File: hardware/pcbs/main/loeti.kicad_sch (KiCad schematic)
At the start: 99 parts, among them J1 REDFIT_SWD_6, J2 DATA, J3 POWER, J4 Conn_01x04_Pin, Q1 Si4162DY, Q2 BC817, Q4 BC817, Q5 BC807, Q6 Si4425FDY, SW1 BOOT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

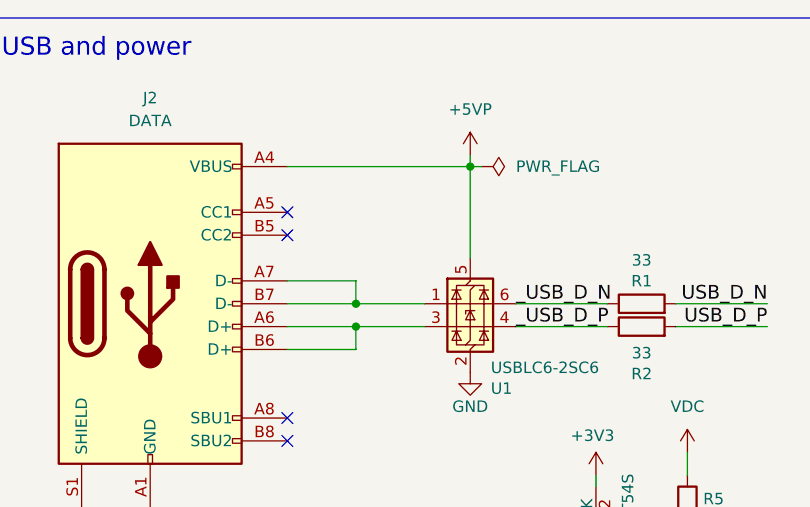
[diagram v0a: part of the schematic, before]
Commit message: fix: v6d hardware, CC resistors on data port
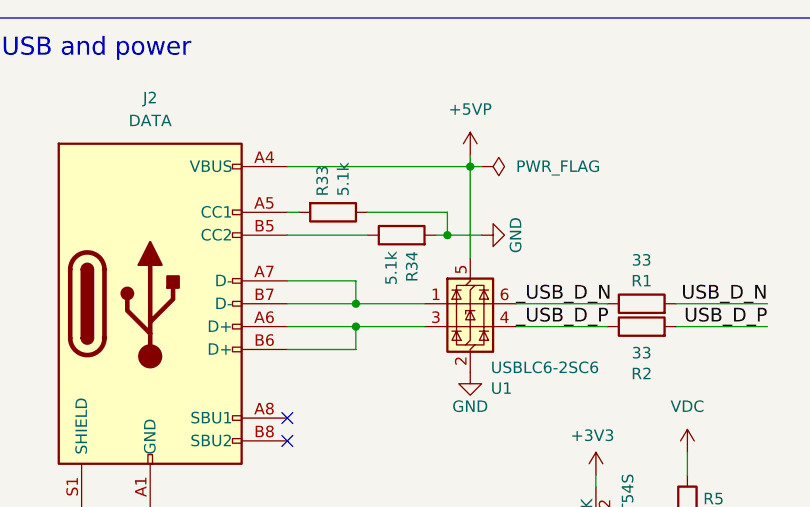
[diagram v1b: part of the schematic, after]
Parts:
- added R33, R34: 5.1k, Resistor_SMD:R_0603_1608Metric, symbol Device:R
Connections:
- net GND: now also R33.1, R34.2
- net at J2.A5 (CC1): now also R33.2
- net at J2.B5 (CC2): now also R34.1
- no-connect marks 22 -> 20

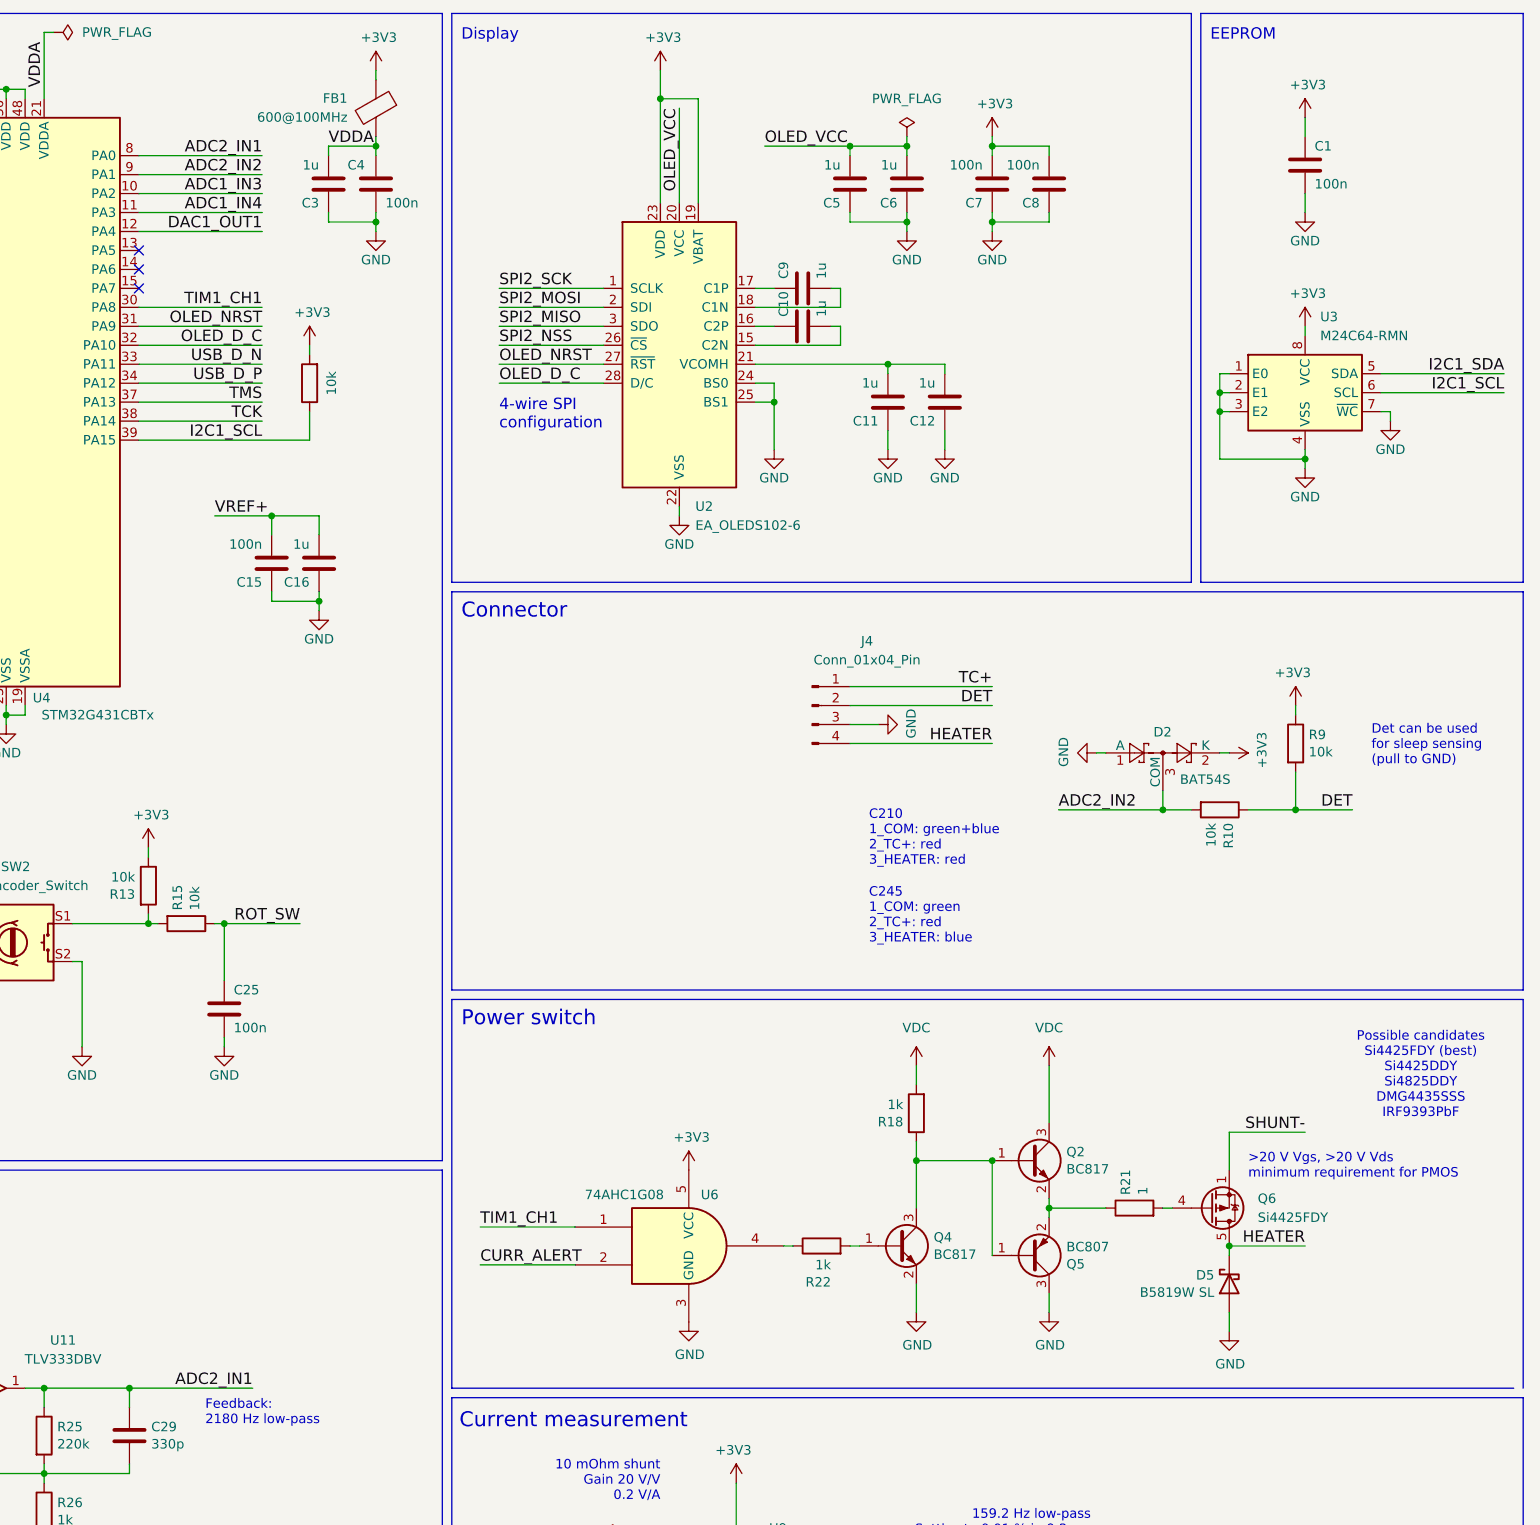
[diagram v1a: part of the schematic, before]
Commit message: feat: sleep support on PCB
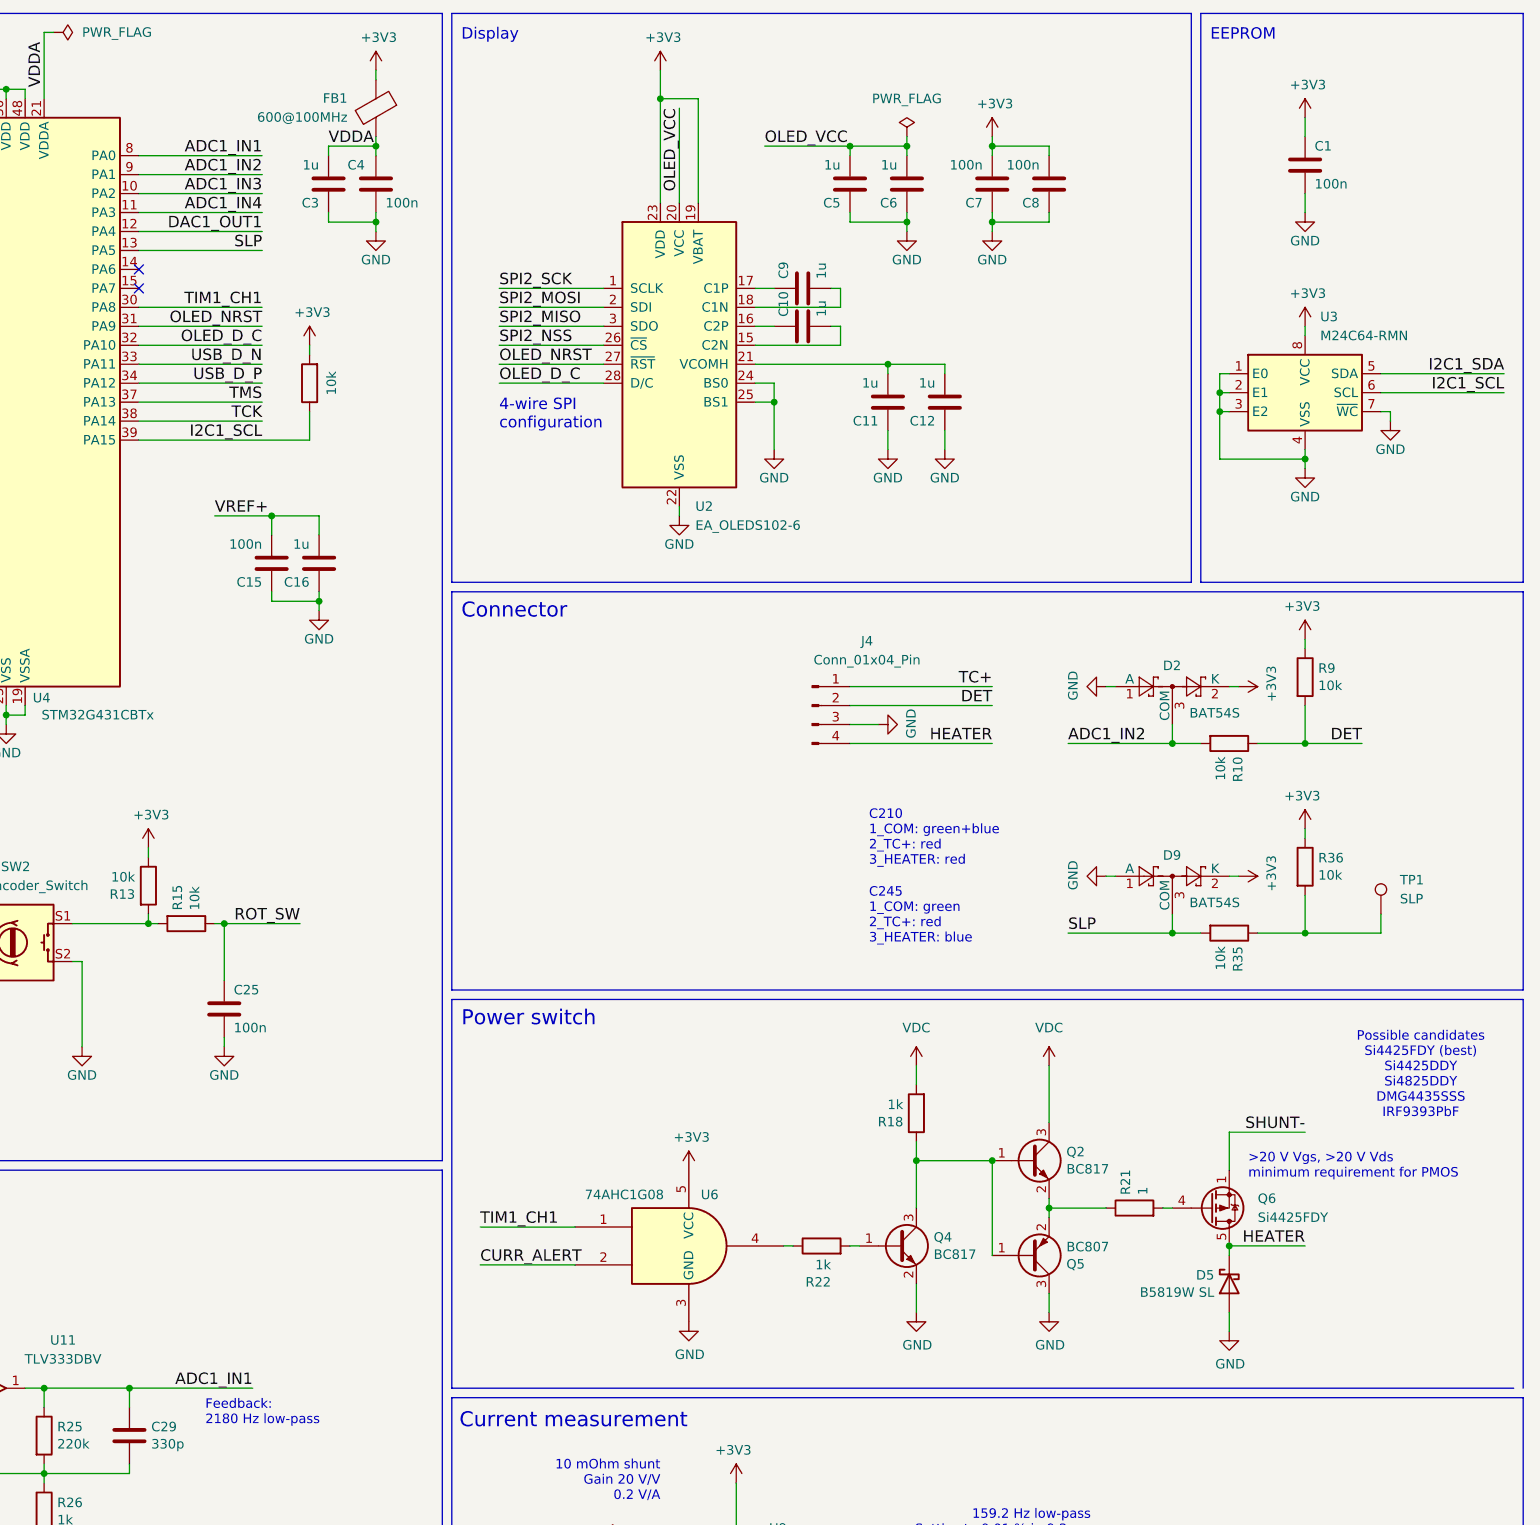
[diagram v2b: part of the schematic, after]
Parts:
- added D9: BAT54S, Package_TO_SOT_SMD:SOT-23, symbol Diode:BAT54S
- added R35, R36: 10k, Resistor_SMD:R_0603_1608Metric, symbol Device:R
- added TP1: SLP, TestPoint:TestPoint_Plated_Hole_D2.0mm, symbol Connector:TestPoint
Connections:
- net +3V3: now also D9.2 (K), R36.1
- net GND: now also D9.1 (A)
- net SLP: now reaches U4.13 (PA5)
- net SLP: now also D9.3 (COM), R35.2
- net ADC2_IN1 renamed ADC1_IN1
- net ADC2_IN2 renamed ADC1_IN2
- new net: R35.1, R36.2, TP1.1
- no-connect marks 20 -> 19
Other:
- note removed: "Det can be used for sleep sensing (pull to GND)"
- moved on the sheet: D2, R10, R9

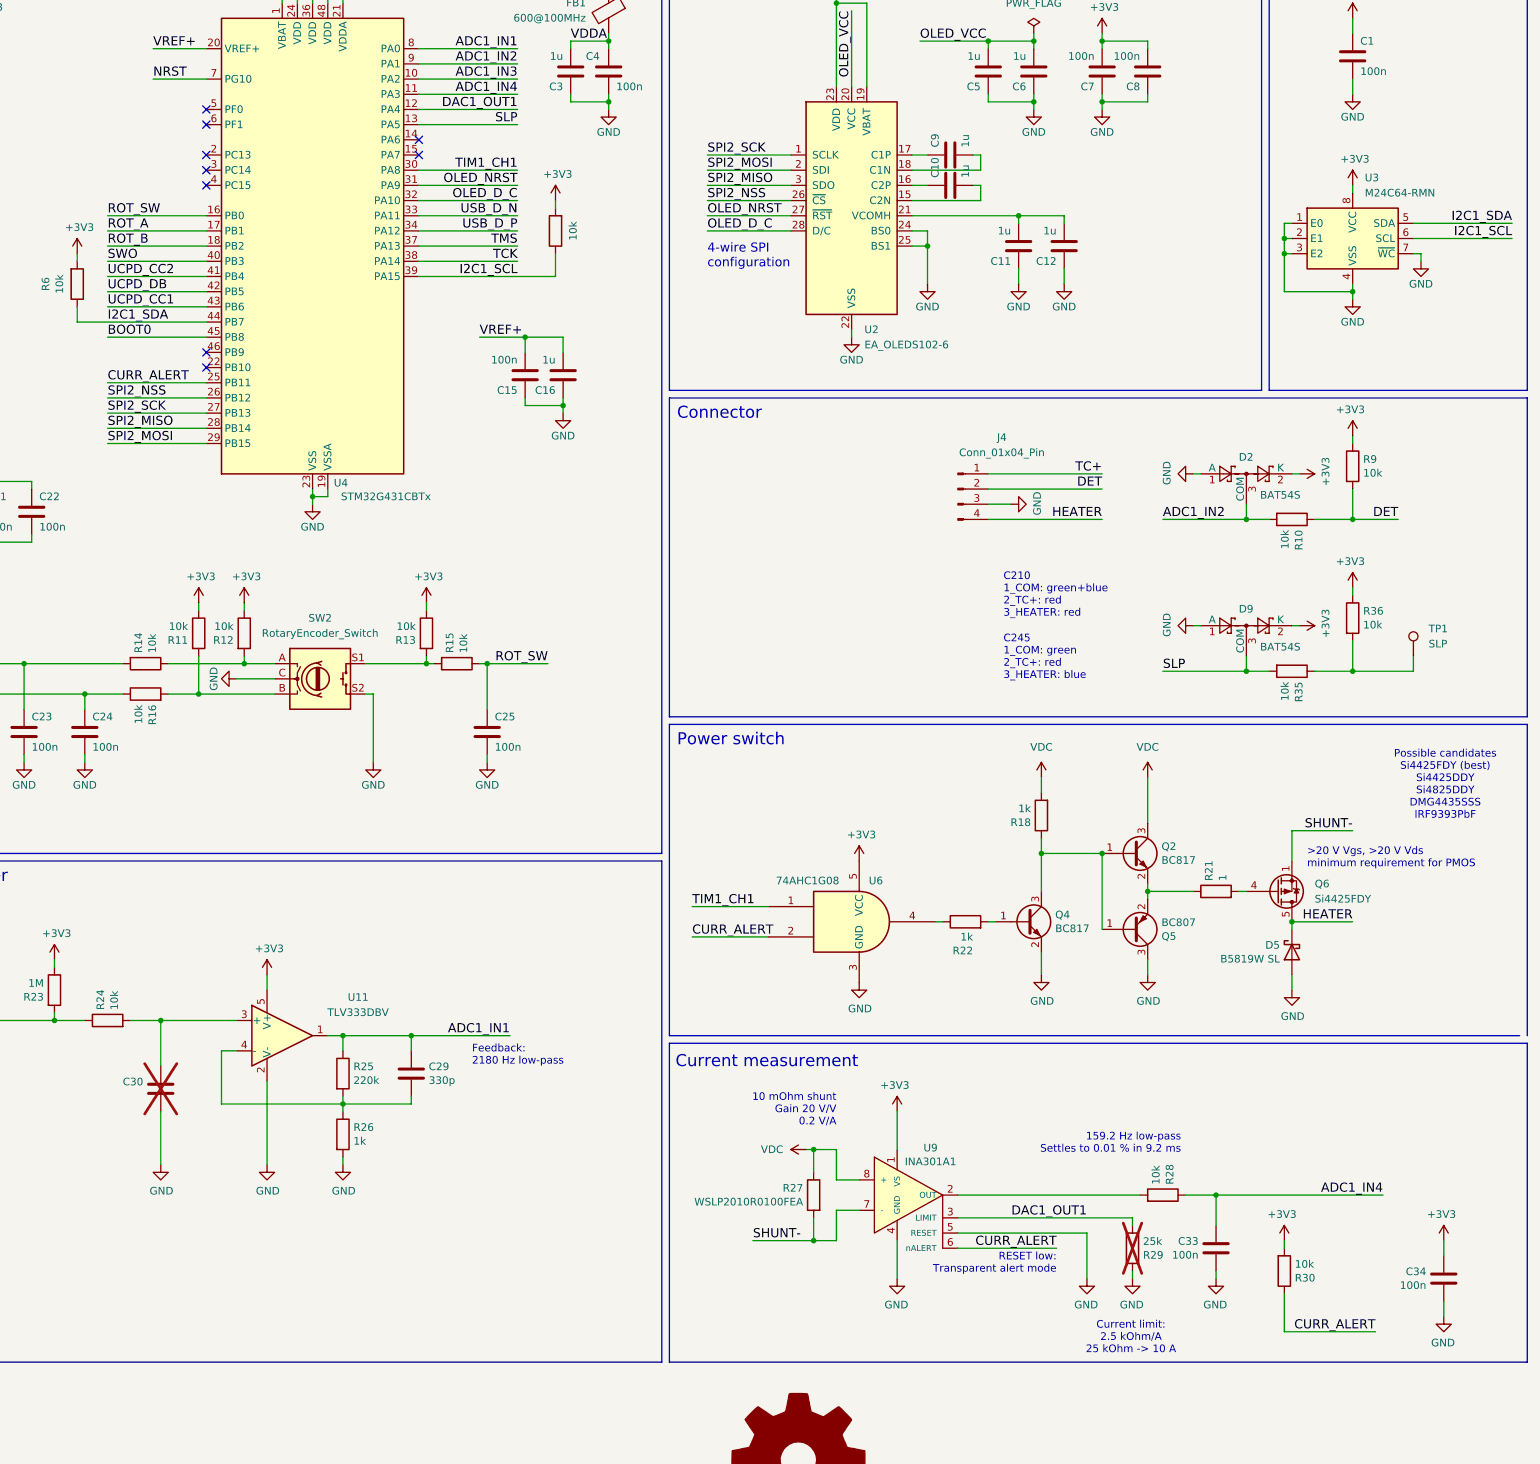
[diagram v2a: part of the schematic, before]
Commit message: feat: update to 5-pin XLR for sleep
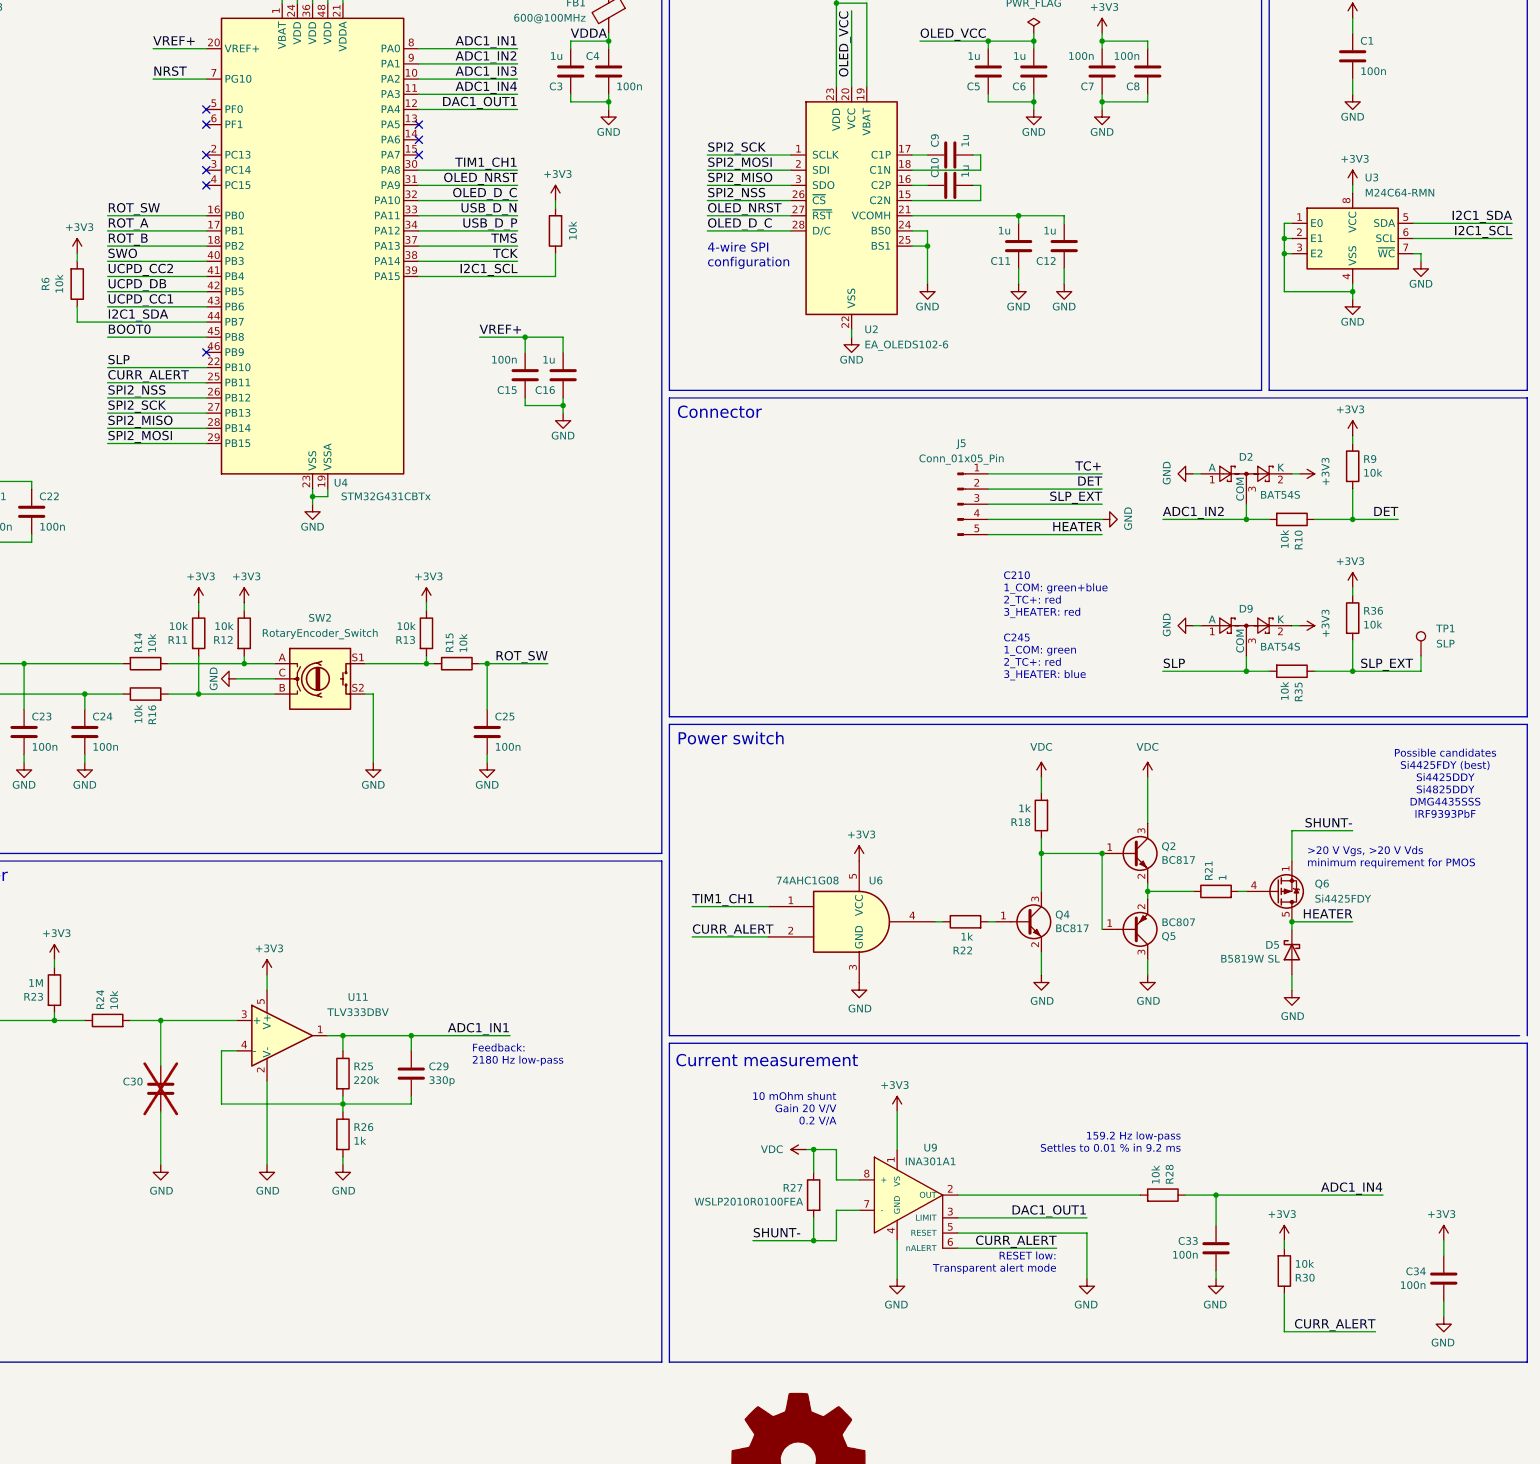
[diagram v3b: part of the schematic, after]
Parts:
- removed J4: Conn_01x04_Pin, Connector_PinHeader_2.54mm:PinHeader_1x04_P2.54mm_Horizontal, symbol Connector:Conn_01x04_Pin
- removed R29: 25k, Resistor_SMD:R_0603_1608Metric, symbol Device:R
- added J5: Conn_01x05_Pin, Connector_PinHeader_2.54mm:PinHeader_1x05_P2.54mm_Horizontal, symbol Connector:Conn_01x05_Pin
- C26: footprint Capacitor_THT:CP_Radial_D10.0mm_P3.50mm -> Capacitor_THT:CP_Radial_D8.0mm_P3.50mm
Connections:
- net DET: now also J5.2 (Pin_2)
- net GND: now also J5.4 (Pin_4)
- net HEATER: now also J5.5 (Pin_5)
- net SLP: now also U4.22 (PB10); no longer U4.13 (PA5)
- net TC+: now also J5.1 (Pin_1)
- net SLP_EXT: now reaches R35.1, R36.2, TP1.1
- net SLP_EXT: now also J5.3 (Pin_3)
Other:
- note removed: "Current limit: 2.5 kOhm/A 25 kOhm -> 10 A"
- moved on the sheet: TP1
